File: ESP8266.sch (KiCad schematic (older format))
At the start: 14 parts, among them P701 CONN_01X06, U701 ESP-12, U702 ISL83485

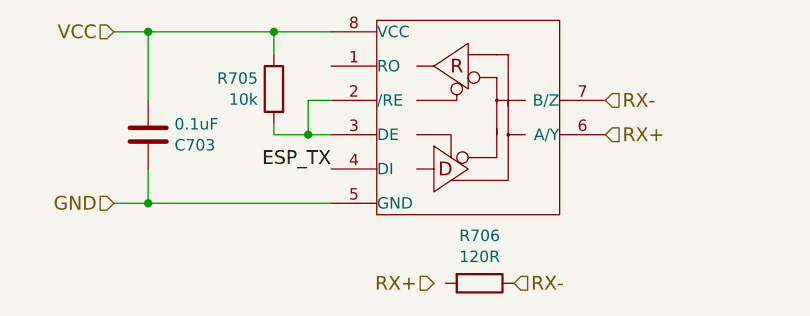
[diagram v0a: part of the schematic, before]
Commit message: Improved connector placement
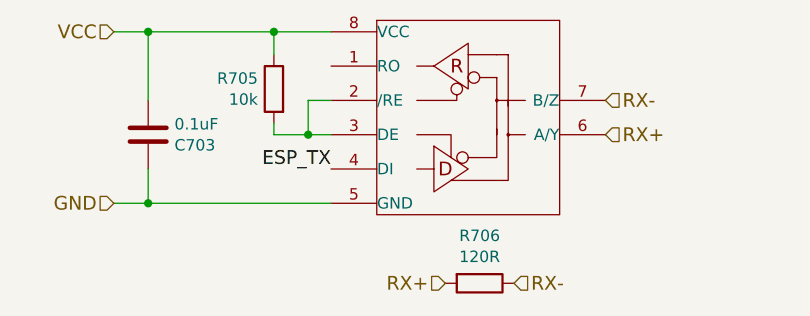
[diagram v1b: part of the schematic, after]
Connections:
- net RX+: now also R706.2
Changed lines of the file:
@@
 Text HLabel 6150 4900 2    60   Input ~ 0
 RX-
-Text HLabel 5800 4900 0    60   Input ~ 0
+Text HLabel 5850 4900 0    60   Input ~ 0
 RX+
 Wire Wire Line
